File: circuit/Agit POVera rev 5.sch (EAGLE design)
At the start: 37 parts, among them IC1 MEGA8-P, J1 AVR_SPI_PRG_6NS, Y2 8Mhz

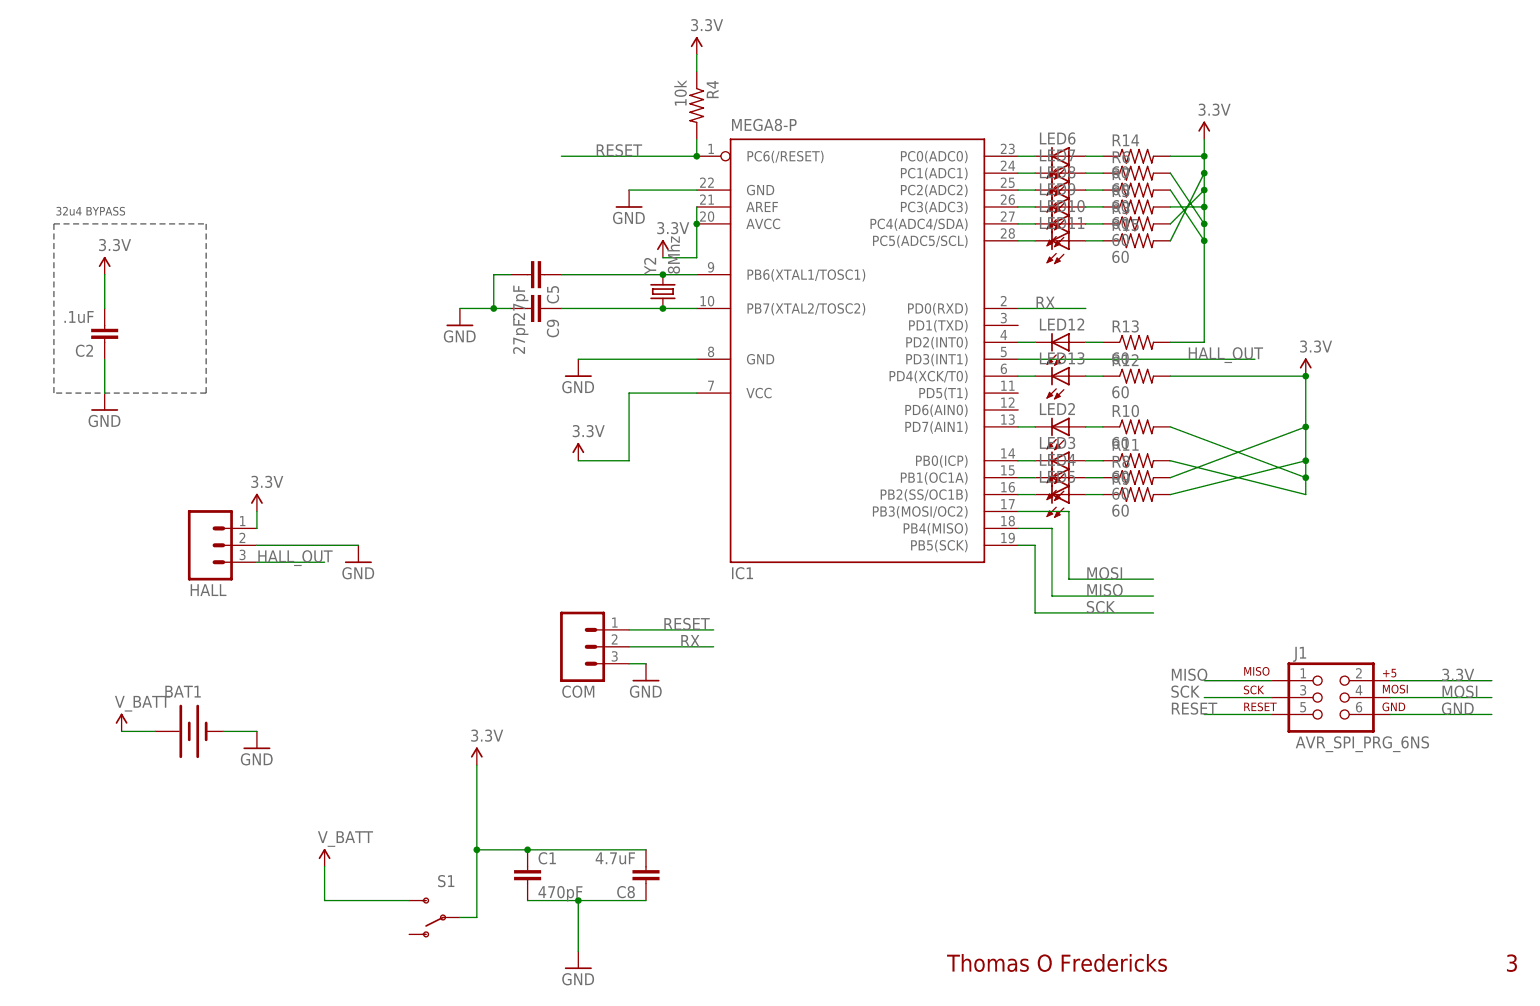
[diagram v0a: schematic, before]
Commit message: Changes for rev 5
Everything new is under ‘circuit’  :
The build guide is updated;
Removed the extra parts in the BOM;
Added the new version of the .brd, .sch and the gerbers for people
wanting to print more from board houses.
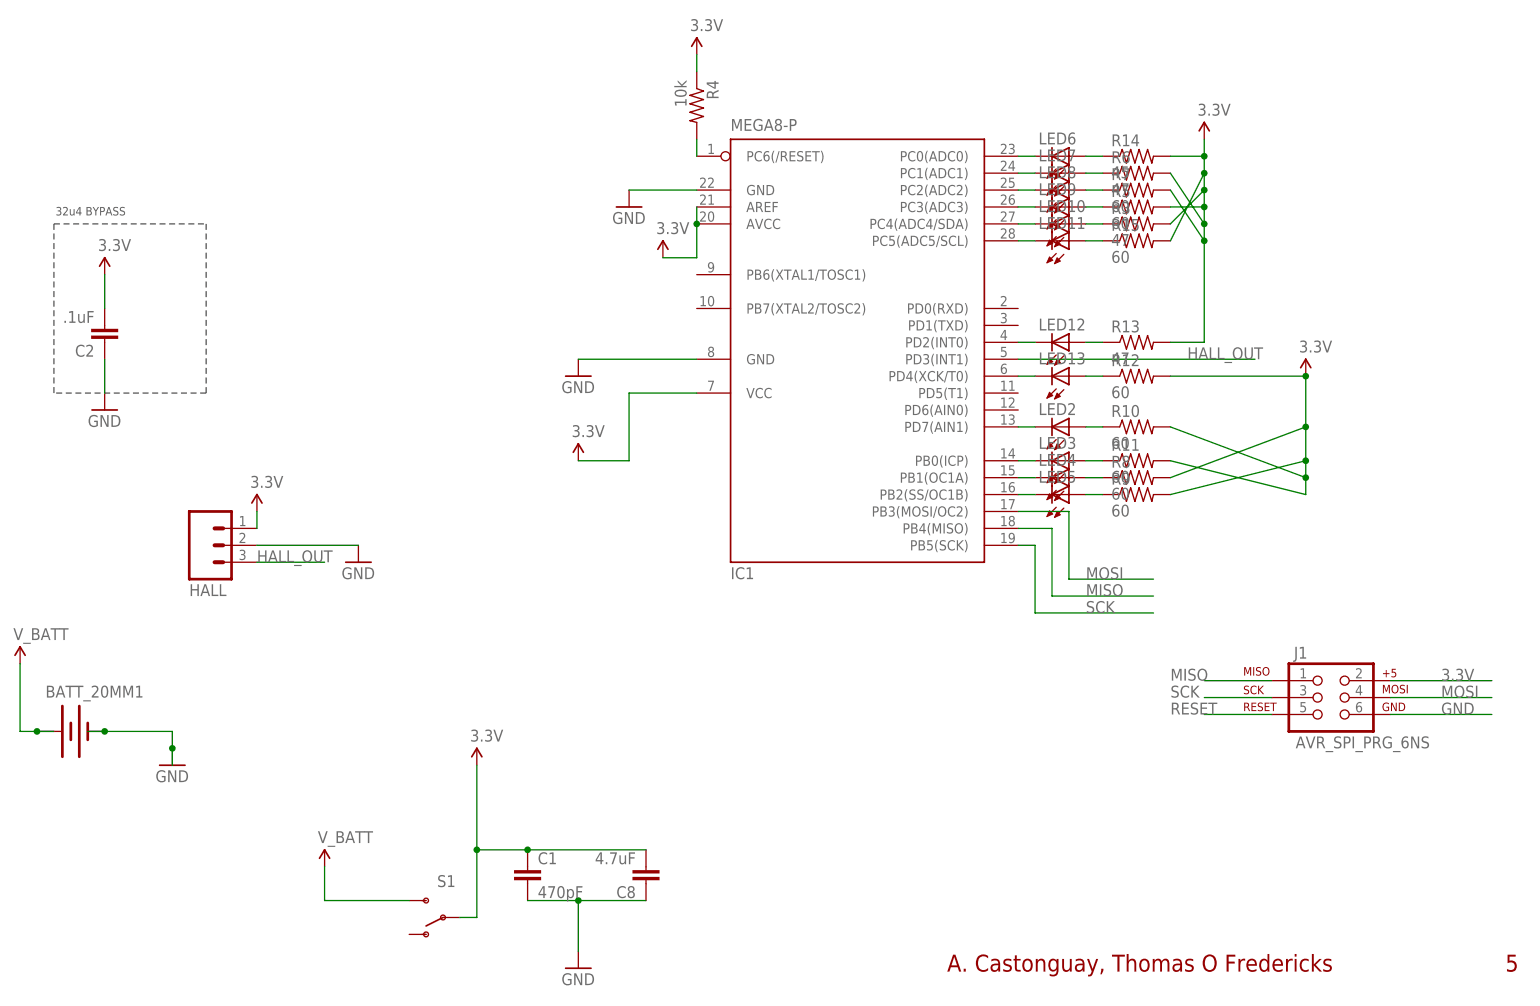
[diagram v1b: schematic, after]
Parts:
- removed BAT1: (no value), SparkFun-Electromechanical:BATTERY20PTH
- removed C5, C9: 27pF, SparkFun-Passives:CAPEZ
- removed COM: (no value), SparkFun-Connectors:M03PTH
- removed Y2: 8Mhz, SparkFun-FreqCtrl:CRYSTALHC49US
- added BATT_20MM1: (no value), User-Submitted:BATTERIE
- R13, R3, R6: value 60 -> 47
- R14: value 60 -> 45
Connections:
- net N$1 renamed LED7
- net N$10 renamed LED4
- net N$11 renamed LED5
- net N$12 renamed LED13
- net N$13 renamed R9
- net N$2 renamed LED8
- net N$21 renamed R7
- net N$3 renamed LED9
- net N$4 renamed LED12
- net N$5 renamed LED10
- net N$6 renamed LED11
- net N$7 renamed LED6
- net N$8 renamed LED2
- net N$9 renamed LED3
- removed net N$34: C5.1, IC1.PB6(XTAL1/TOSC1), Y2.2
- removed net N$35: C9.1, IC1.PB7(XTAL2/TOSC2), Y2.1
- removed net RX: COM.2, IC1.PD0(RXD)
- net GND: now also BATT_20MM1.-; no longer BAT1.-, C5.2, C9.2, COM.3
- net RESET: no longer COM.1
- net V_BATT: now also BATT_20MM1.+; no longer BAT1.+
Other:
- note added: "5"
- note added: "A. Castonguay, Thomas O Fredericks"
- note removed: "3"
- note removed: "Thomas O Fredericks"
